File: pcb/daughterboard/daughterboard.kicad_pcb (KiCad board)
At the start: 2 copper layers, 51 parts, among them IC1 TLE94112ESXUMA1, IC2 TLE94112ESXUMA1, IC3 TLE94112ESXUMA1, IC4 TLE94112ESXUMA1, IC5 TLE94112ESXUMA1, IC6 TLE94112ESXUMA1, IC7 TLE94112ESXUMA1, J1 Conn_01x20_Pin, J10 Conn_01x04_Socket, J11 Conn_01x04_Socket, J12 Conn_01x04_Socket, J13 Conn_01x04_Socket, J14 Conn_01x04_Socket, J15 Conn_01x04_Socket, J16 Conn_01x04_Socket, J17 Conn_01x04_Socket, J18 Conn_01x04_Socket, J19 Conn_01x04_Socket, J2 Conn_01x04_Socket, J20 Conn_01x04_Socket, J21 Conn_01x04_Socket, J22 Conn_01x20_Pin, J3 Conn_01x04_Socket, J4 Conn_01x04_Socket, J5 Conn_01x04_Socket, J6 Conn_01x04_Socket, J7 Conn_01x04_Socket, J8 Conn_01x04_Socket, J9 Conn_01x04_Socket

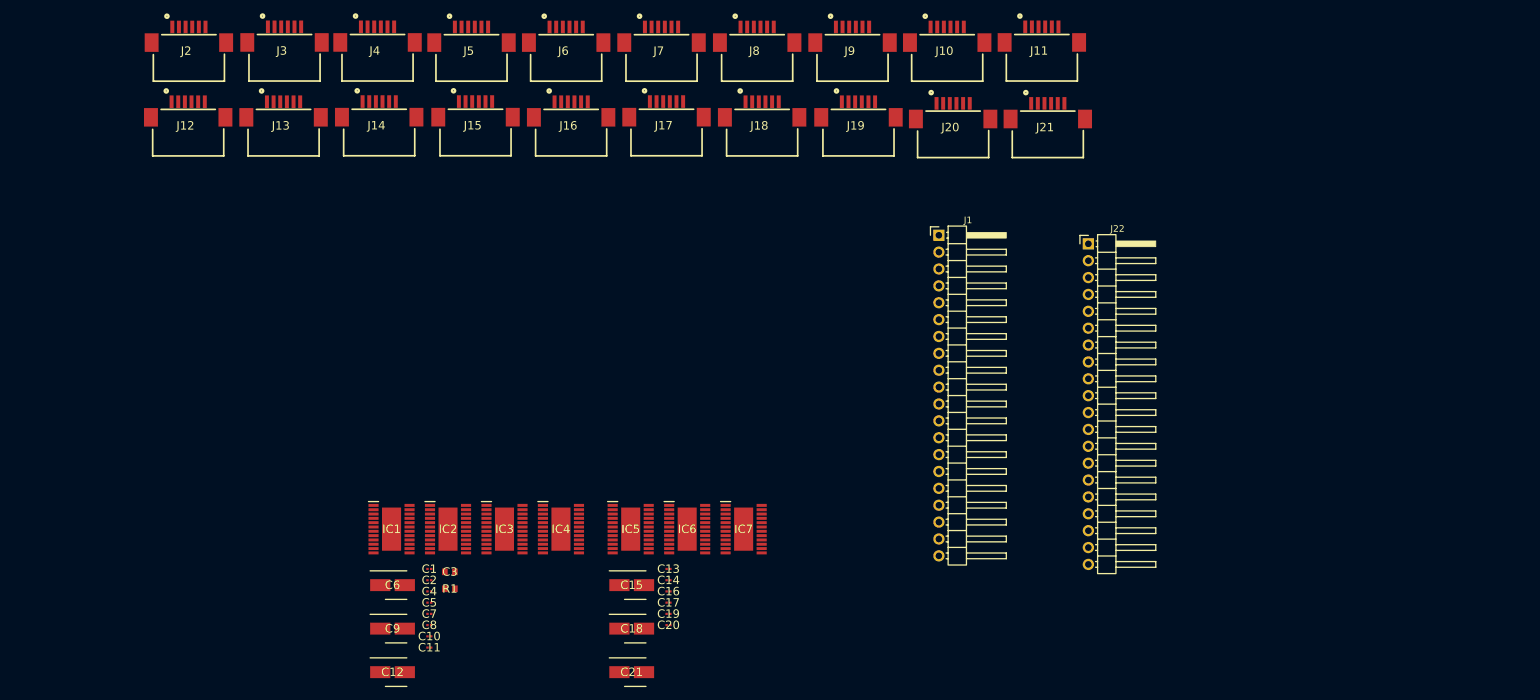
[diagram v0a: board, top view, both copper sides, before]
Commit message: initial design & routed decoupling capacitors
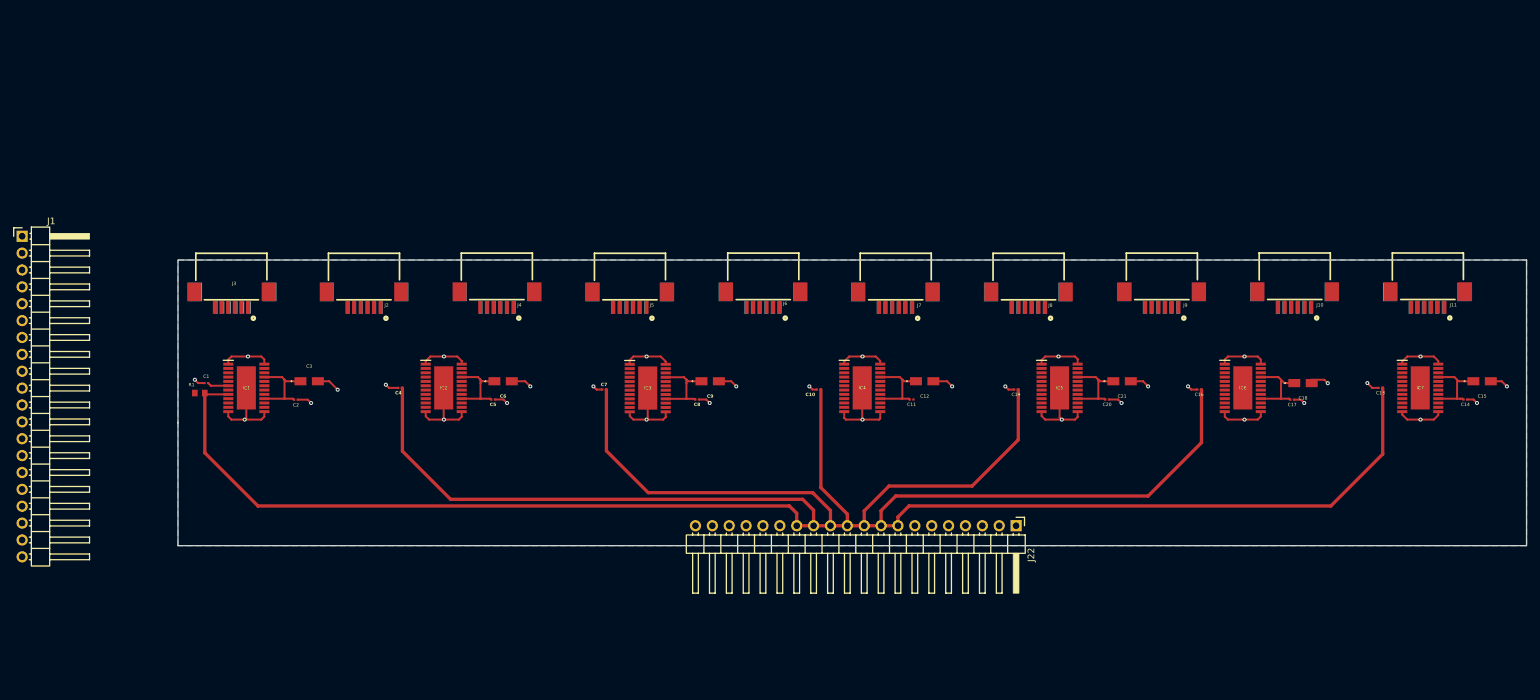
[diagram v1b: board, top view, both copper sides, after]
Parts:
- C12, C15, C18, C21, C6, C9: footprint A_HANU_FOOTPRINTS:CAPAE430X550N -> A_HANU_FOOTPRINTS:T491A
- C3: footprint A_HANU_FOOTPRINTS:RESC1608X50N -> A_HANU_FOOTPRINTS:T491A
- J12, J13, J14, J15, J16, J17, J18, J19, J20, J21: moved to B.Cu
- moved J1 138.0 mm to (34.5, 64.9)
- moved C15 131.6 mm to (254.3, 86.7)
- moved C14 123.0 mm to (251.7, 89.5)
- moved C13 110.6 mm to (239.0, 87.7), turned to 180 degrees
- moved C18 107.6 mm to (227.3, 87.0)
- moved IC7 104.0 mm to (245.0, 87.7)
- moved C17 98.7 mm to (225.7, 89.5)
- moved C12 91.3 mm to (170.4, 86.7)
- moved IC6 86.3 mm to (218.2, 87.7)
- moved C21 85.8 mm to (200.1, 86.7)
- moved C16 85.5 mm to (211.7, 88.0), turned to 180 degrees
- moved C11 81.6 mm to (168.4, 89.5)
- moved C20 74.2 mm to (197.8, 89.5)
- moved J11 71.8 mm to (246.1, 75.6), turned to 180 degrees
- moved C10 69.4 mm to (154.4, 88.0), turned to 180 degrees
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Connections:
- C13 pad 1: /drivers2/+3.3V -> +3.3V
- C14 pad 1: /drivers2/+9V -> +9V
- C15 pad 1: /drivers2/+9V -> +9V
- C16 pad 1: /drivers2/+3.3V -> +3.3V
- C17 pad 1: /drivers2/+9V -> +9V
- C18 pad 1: /drivers2/+9V -> +9V
- C19 pad 1: /drivers2/+3.3V -> +3.3V
- C20 pad 1: /drivers2/+9V -> +9V
- C21 pad 1: /drivers2/+9V -> +9V
- IC5 pad 16: /drivers2/+9V -> +9V
- IC5 pad 21: /drivers2/+9V -> +9V
- IC5 pad 6: /drivers2/+3.3V -> +3.3V
- IC5 pad 8: /drivers2/+3.3V -> +3.3V
- IC6 pad 16: /drivers2/+9V -> +9V
- IC6 pad 21: /drivers2/+9V -> +9V
- IC6 pad 6: /drivers2/+3.3V -> +3.3V
- IC6 pad 8: /drivers2/+3.3V -> +3.3V
- IC7 pad 16: /drivers2/+9V -> +9V
- IC7 pad 21: /drivers2/+9V -> +9V
- IC7 pad 6: /drivers2/+3.3V -> +3.3V
- IC7 pad 8: /drivers2/+3.3V -> +3.3V
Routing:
- net +3.3V: track 0.00 -> 462.7 mm
- net GND: track 0.00 -> 168.7 mm, vias 0 -> 34
- net +9V: track 0.00 -> 89.3 mm
- added copper zone on B.Cu, net GND
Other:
- board outline added: 203 x 43 mm
